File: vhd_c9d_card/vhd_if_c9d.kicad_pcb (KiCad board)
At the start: 2 copper layers, 145 x 120 mm, 76 parts, among them IC1 80C49C, IC10 74LS04, IC11 SN751701P, IC12 74H004P, IC2 8255A, IC3 27C256, IC5 74LS30, IC6 74LS30, IC7 74LS27, IC8 74LS32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

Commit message: Add files via upload
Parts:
- removed L3: L, Inductor_THT:L_Axial_L5.0mm_D3.6mm_P10.00mm_Horizontal_Murata_BL01RN1A2A2
- added FL6: EMI_Filter_LCL, Connector_PinHeader_2.54mm:PinHeader_1x03_P2.54mm_Vertical, F.Cu at (165.3, 122.7)
- added FL7: EMI_Filter_LCL, Connector_PinHeader_2.54mm:PinHeader_1x03_P2.54mm_Vertical, F.Cu at (165.4, 126.4)
- added FL8: EMI_Filter_LCL, Connector_PinHeader_2.54mm:PinHeader_1x03_P2.54mm_Vertical, F.Cu at (169.7, 56.7)
- added FL9: EMI_Filter_LCL, Connector_PinHeader_2.54mm:PinHeader_1x03_P2.54mm_Vertical, F.Cu at (169.5, 60.2)
- moved L1 79.5 mm to (175.8, 52.7)
- moved FL4 7.44 mm to (170.8, 130.3)
- moved R4 5.13 mm to (175.3, 41.4)
- moved R9 2.97 mm to (160.1, 122.0)
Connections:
- J2 pad 1: A1 -> Net-(J2-Pad1)
- J2 pad 2: S2 -> Net-(FL8-Pad3)
- J2 pad 3: S3 -> Net-(FL9-Pad3)
- J2 pad 7: A1 -> Net-(J2-Pad1)
- J3 pad 7: Net-(J3-Pad7) -> Net-(FL7-Pad3)
- L1 pad 1: Net-(J3-Pad7) -> Net-(J2-Pad1)
- L1 pad 2: VHD7 -> A1
- Q1 pad 2: A1 -> B8
- Q1 pad 3: B8 -> A1
- Q2 pad 2: A1 -> Net-(D3-Pad2)
- Q2 pad 3: Net-(D3-Pad2) -> A1
- Q3 pad 2: A26 -> A1
- Q3 pad 3: A1 -> A26
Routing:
- net C21: track 133.6 -> 184.0 mm
- net B22: track 188.7 -> 140.3 mm, vias 0 -> 1
- net Net-(IC2-Pad5): track 75.3 -> 112.5 mm
- net Net-(IC6-Pad8): track 120.8 -> 86.4 mm, vias 1 -> 2
- net Net-(J3-Pad7): track 30.6 -> 0.00 mm
- net Net-(IC9-Pad1): track 138.6 -> 108.3 mm, vias 1 -> 2
- net Net-(IC1-Pad35): track 67.5 -> 39.6 mm, vias 0 -> 1
- net B12: track 129.9 -> 157.2 mm, vias 1 -> 0
- net B29: track 595.0 -> 569.3 mm
- net Net-(FL7-Pad3): track 0.00 -> 23.7 mm
- net B24: track 103.1 -> 126.0 mm
- net Net-(IC2-Pad36): track 88.8 -> 66.2 mm
- net C24: track 106.6 -> 128.6 mm, vias 2 -> 1
- net B13: track 104.5 -> 84.2 mm
- net Net-(FL4-Pad3): track 42.6 -> 59.8 mm
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- added copper zone on B.Cu, net A1
- removed copper zone on B.Cu, net B29

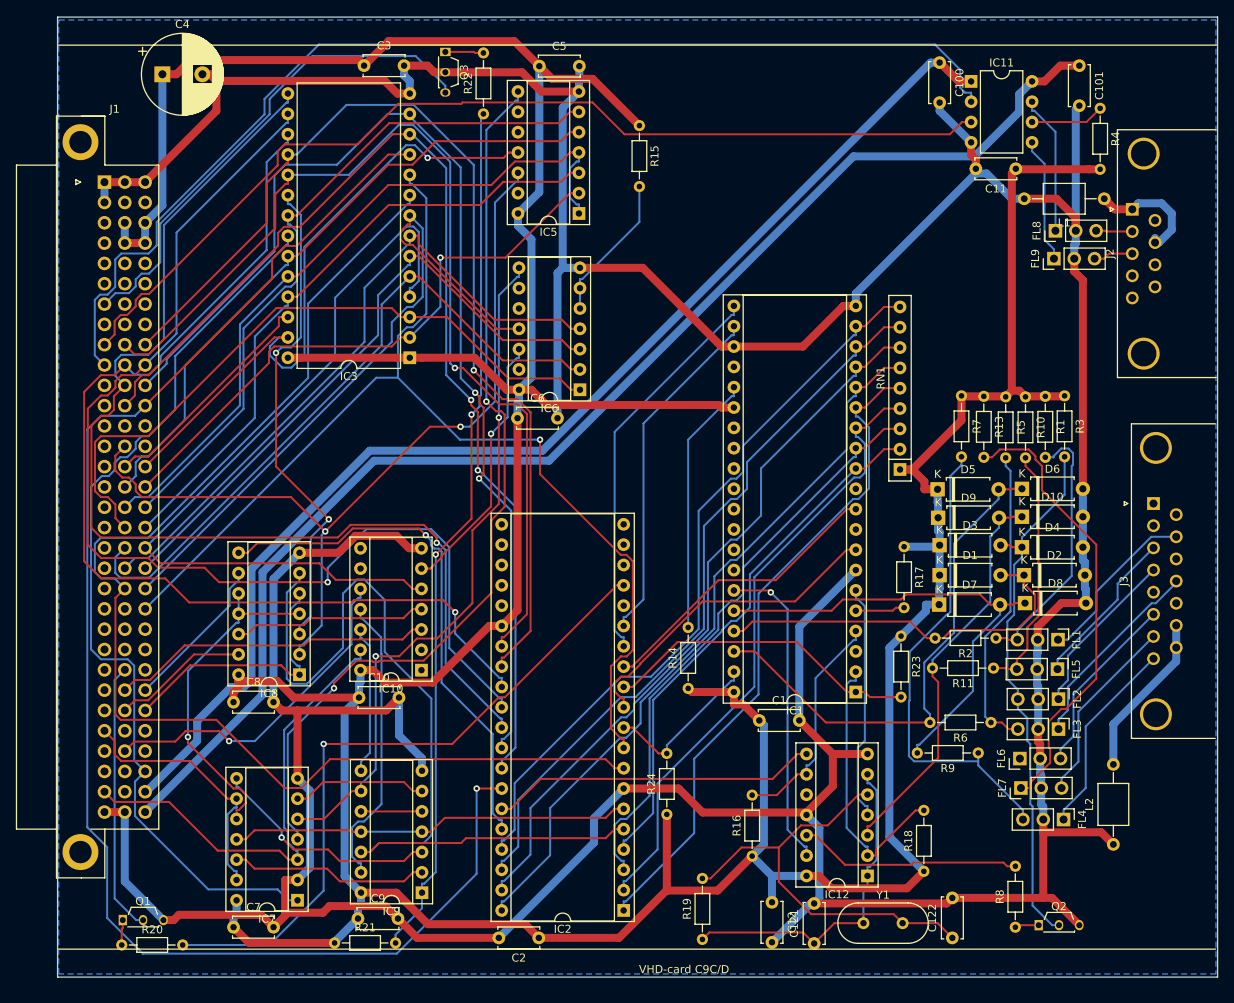
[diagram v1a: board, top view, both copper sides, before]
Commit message: Add files via upload
now reset line is also connected in pcb and some component movement done near crystal.
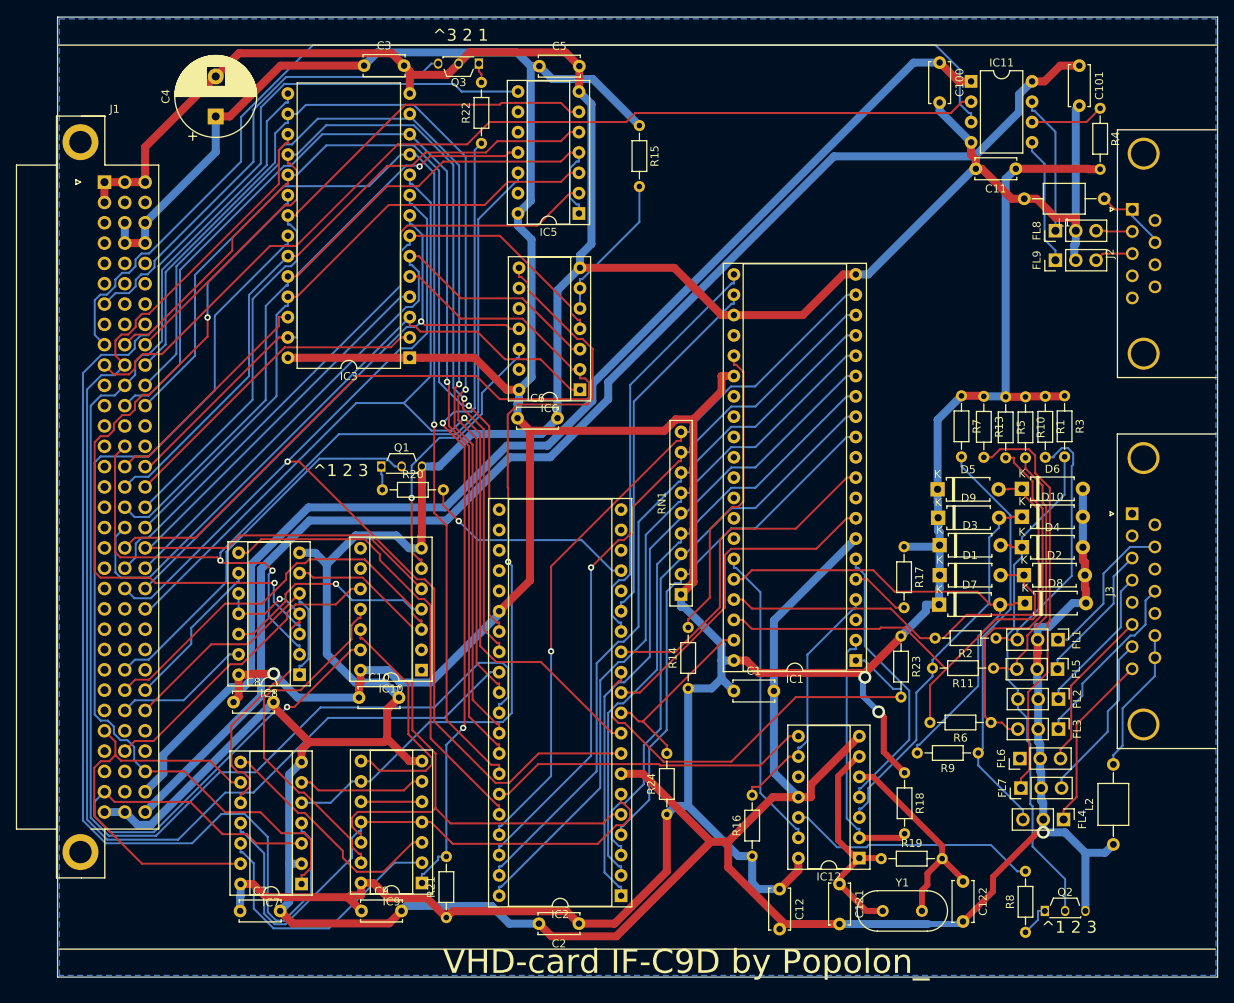
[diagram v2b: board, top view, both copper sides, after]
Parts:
- J3: footprint Connector_Dsub:DSUB-15_Female_Horizontal_P2.77x2.84mm_EdgePinOffset4.94mm_Housed_MountingHolesOffset7.48mm -> Connector_Dsub:DSUB-15_Female_Horizontal_P2.77x2.84mm_EdgePinOffset7.70mm_Housed_MountingHolesOffset9.12mm
- moved R20 65.6 mm to (85.6, 89.1)
- moved Q1 65.3 mm to (85.5, 86.2)
- moved RN1 31.5 mm to (122.9, 102.2)
- moved R19 24.5 mm to (148.0, 135.2), turned to 0 degrees
- moved R21 14.3 mm to (93.6, 142.6), turned to 90 degrees
- moved R18 12.6 mm to (150.9, 124.5), turned to 270 degrees
- moved C4 8.50 mm to (64.8, 42.4), turned to 90 degrees
- moved C121 8.08 mm to (142.7, 138.4), turned to 270 degrees
- moved C122 7.17 mm to (158.2, 138.0), turned to 270 degrees
- moved C2 5.32 mm to (110.2, 143.3)
- moved C1 4.86 mm to (129.5, 114.2)
- moved Q3 4.44 mm to (97.7, 35.8), turned to 180 degrees
- moved IC1 3.94 mm to (144.8, 110.4)
- moved R22 3.69 mm to (98.0, 45.8)
- moved J3 2.95 mm to (179.3, 92.1)
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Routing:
- net Net-(IC5-Pad8): track 113.5 -> 187.7 mm, vias 2 -> 0
- net Net-(IC2-Pad17): track 84.6 -> 27.6 mm
- net C21: track 184.0 -> 135.1 mm
- net Net-(IC2-Pad5): track 112.5 -> 79.8 mm
- net B23: track 129.8 -> 160.4 mm, vias 1 -> 0
- net B22: track 140.3 -> 170.9 mm, vias 1 -> 0
- net Net-(IC3-Pad20): track 62.1 -> 89.7 mm
- net Net-(C122-Pad1): track 53.9 -> 27.0 mm
- net Net-(IC2-Pad6): track 50.1 -> 72.5 mm
- net B29: track 569.3 -> 550.7 mm, vias 0 -> 3
- net A5: track 32.4 -> 50.8 mm
- net A23: track 141.2 -> 123.4 mm
- net B12: track 157.2 -> 139.9 mm, vias 0 -> 1
- net C14: track 100.9 -> 84.0 mm
- net T0_PC5: track 39.9 -> 56.1 mm
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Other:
- net class CLK added: clearance 0.25, trace_width 0.75, via_dia 1, via_drill 0.6
- board text added: "VHD-card IF-C9D by Popolon_"
- board text added: "^1 2 3"
- board text added: "^3 2 1"
- board text removed: "VHD-card C9C/D"

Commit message: Add files via upload
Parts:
- removed R1, R10, R13, R3, R5, R7: 4K7, Resistor_THT:R_Axial_DIN0204_L3.6mm_D1.6mm_P7.62mm_Horizontal
- added RN2: 8x4K7, Resistor_THT:R_Array_SIP9, F.Cu at (153.7, 80.0)
- IC2: value 8255A -> NEC D8255AC-2
- R19: value 750K -> 1M
- R4: value 10K -> 27K
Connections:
- net Net-(D3-Pad2) renamed VHD4PULLUP
- net Net-(FL1-Pad3) renamed VHD10PULLUP
- net Net-(FL3-Pad3) renamed VHD12PULLUP
- net Net-(FL4-Pad3) renamed VHD8PULLUP
- net Net-(FL5-Pad3) renamed VHD3PULLUP
- IC1 pad 4: RESET_ -> A6
- IC12 pad 9: RESET_ -> A6
- J1 pad A6: (no net) -> A6
- R16 pad 2: RESET_ -> A6
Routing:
- net A6: track 0.00 -> 139.1 mm
- net B23: track 160.4 -> 120.5 mm, vias 0 -> 1
- net B22: track 170.9 -> 139.4 mm, vias 0 -> 1
- net RESET_: track 31.3 -> 0.00 mm
- net Net-(IC2-Pad6): track 72.5 -> 50.2 mm
- net Net-(IC5-Pad8): track 187.7 -> 166.5 mm
- net B13: track 84.2 -> 105.0 mm
- net Net-(IC9-Pad1): track 99.8 -> 119.6 mm, vias 2 -> 1
- net A5: track 50.8 -> 31.5 mm
- net T0_PC5: track 56.1 -> 38.5 mm
- net A23: track 123.4 -> 138.7 mm
- net Net-(IC2-Pad36): track 58.4 -> 72.0 mm, vias 0 -> 1
- net VHD3PULLUP: track 32.0 -> 45.0 mm
- net C23: track 134.0 -> 121.1 mm
- net C24: track 120.5 -> 107.8 mm
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
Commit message: Add files via upload
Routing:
- net Net-(IC12-Pad12): track 31.6 -> 50.3 mm
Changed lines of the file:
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@@
     (thickness 1.6)
     (drawings 10)
-    (tracks 1601)
+    (tracks 1606)
     (zones 0)
     (modules 74)
@@
   )
   (setup
-    (last_trace_width 0.75)
+    (last_trace_width 0.25)
     (user_trace_width 0.25)
     (user_trace_width 0.75)
@@
   (segment (start 137.604 130.048) (end 138.7293 130.048) (width 0.25) (layer F.Cu) (net 93))
   (segment (start 138.7293 130.048) (end 138.7293 130.7513) (width 0.25) (layer F.Cu) (net 93))
-  (segment (start 138.7293 130.7513) (end 144.757 136.779) (width 0.25) (layer F.Cu) (net 93))
-  (segment (start 144.757 136.779) (end 165.989 136.779) (width 0.25) (layer F.Cu) (net 93))
+  (segment (start 139.21225 131.23425) (end 139.21225 144.54625) (width 0.25) (layer F.Cu) (net 93))
+  (segment (start 138.7293 130.7513) (end 139.21225 131.23425) (width 0.25) (layer F.Cu) (net 93))
+  (segment (start 139.21225 144.54625) (end 140.716 146.05) (width 0.25) (layer F.Cu) (net 93))
+  (segment (start 140.716 146.05) (end 162.306 146.05) (width 0.25) (layer F.Cu) (net 93))
+  (segment (start 162.306 146.05) (end 164.084 144.272) (width 0.25) (layer F.Cu) (net 93))
+  (segment (start 164.084 138.684) (end 165.989 136.779) (width 0.25) (layer F.Cu) (net 93))
+  (segment (start 164.084 144.272) (end 164.084 138.684) (width 0.25) (layer F.Cu) (net 93))
   (segment (start 155.575 138.049) (end 155.575 135.192) (width 0.25) (layer B.Cu) (net 94))
   (segment (start 153.046 141.732) (end 155.575 139.203) (width 0.25) (layer B.Cu) (net 94))

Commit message: Add files via upload
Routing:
- net Net-(J3-Pad14): track 18.3 -> 20.1 mm
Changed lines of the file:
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@@
     (thickness 1.6)
     (drawings 10)
-    (tracks 1606)
+    (tracks 1613)
     (zones 0)
     (modules 74)
@@
   )
   (setup
-    (last_trace_width 0.25)
+    (last_trace_width 0.75)
     (user_trace_width 0.25)
     (user_trace_width 0.75)
@@
   (segment (start 161.354 80.01) (end 161.354 81.1353) (width 0.25) (layer B.Cu) (net 65))
   (segment (start 165.418 126.365) (end 165.418 125.1897) (width 0.25) (layer B.Cu) (net 65))
-  (segment (start 182.164 107.31) (end 182.164 110.08) (width 0.25) (layer B.Cu) (net 66))
-  (segment (start 176.974 123.414) (end 176.974 122.2387) (width 0.25) (layer B.Cu) (net 66))
-  (segment (start 176.974 122.2387) (end 178.3659 120.8468) (width 0.25) (layer B.Cu) (net 66))
-  (segment (start 178.3659 120.8468) (end 178.3659 116.1624) (width 0.25) (layer B.Cu) (net 66))
-  (segment (start 178.3659 116.1624) (end 182.164 112.3643) (width 0.25) (layer B.Cu) (net 66))
-  (segment (start 182.164 112.3643) (end 182.164 110.08) (width 0.25) (layer B.Cu) (net 66))
+  (segment (start 176.974 122.2387) (end 178.3659 120.8468) (width 0.75) (layer B.Cu) (net 66))
+  (segment (start 176.974 123.414) (end 176.974 122.2387) (width 0.75) (layer B.Cu) (net 66))
+  (segment (start 178.3659 120.8468) (end 177.9968 120.8468) (width 0.75) (layer B.Cu) (net 66))
+  (segment (start 177.9968 120.8468) (end 176.9745 119.8245) (width 0.75) (layer B.Cu) (net 66))
+  (segment (start 176.9745 119.8245) (end 176.9745 117.221) (width 0.75) (layer B.Cu) (net 66))
+  (segment (start 176.9745 117.221) (end 181.864 112.3315) (width 0.75) (layer B.Cu) (net 66))
+  (segment (start 181.864 110.38) (end 182.164 110.08) (width 0.75) (layer B.Cu) (net 66))
+  (segment (start 181.864 112.3315) (end 181.864 110.38) (width 0.75) (layer B.Cu) (net 66))
+  (segment (start 182.164 110.08) (end 182.164 109.774) (width 0.75) (layer B.Cu) (net 66))
+  (segment (start 182.164 109.774) (end 181.61 109.22) (width 0.75) (layer B.Cu) (net 66))
+  (segment (start 181.61 107.864) (end 182.164 107.31) (width 0.75) (layer B.Cu) (net 66))
+  (segment (start 181.61 109.22) (end 181.61 107.864) (width 0.75) (layer B.Cu) (net 66))
   (segment (start 55.9435 126.83) (end 65.0681 117.7054) (width 1) (layer B.Cu) (net 67))
   (segment (start 65.0681 117.7054) (end 65.0681 115.3634) (width 1) (layer B.Cu) (net 67))
@@
   (segment (start 170.37 122.682) (end 170.37 121.5067) (width 0.25) (layer B.Cu) (net 99))
   (segment (start 179.324 108.695) (end 178.1408 109.8782) (width 0.25) (layer B.Cu) (net 100))
-  (segment (start 178.1408 109.8782) (end 178.1408 115.6828) (width 0.25) (layer B.Cu) (net 100))
-  (segment (start 178.1408 115.6828) (end 177.6906 116.133) (width 0.25) (layer B.Cu) (net 100))
-  (segment (start 177.6906 116.133) (end 177.6906 117.9971) (width 0.25) (layer B.Cu) (net 100))
-  (segment (start 177.6906 117.9971) (end 170.498 125.1897) (width 0.25) (layer B.Cu) (net 100))
   (segment (start 170.498 126.365) (end 170.498 125.1897) (width 0.25) (layer B.Cu) (net 100))
+  (segment (start 178.1408 114.6408) (end 178.0307 114.6408) (width 0.25) (layer B.Cu) (net 100))
+  (segment (start 178.1408 109.8782) (end 178.1408 114.6408) (width 0.25) (layer B.Cu) (net 100))
+  (segment (start 173.0375 119.634) (end 173.0375 122.4915) (width 0.25) (layer B.Cu) (net 100))
+  (segment (start 178.0307 114.6408) (end 173.0375 119.634) (width 0.25) (layer B.Cu) (net 100))
+  (segment (start 173.0375 122.4915) (end 170.498 125.1897) (width 0.25) (layer B.Cu) (net 100))
   (segment (start 174.816 56.7055) (end 175.9913 56.7055) (width 0.25) (layer B.Cu) (net 101))
   (segment (start 179.341 56.799) (end 176.0848 56.799) (width 0.25) (layer B.Cu) (net 101))
@@
     (polygon
       (pts
-        (xy 189.865 149.7965) (xy 45.212 149.7965) (xy 45.212 30.226) (xy 189.865 30.226)
+        (xy 189.4205 149.6695) (xy 45.2755 149.6695) (xy 45.2755 30.4165) (xy 189.4205 30.4165)
       )
     )
